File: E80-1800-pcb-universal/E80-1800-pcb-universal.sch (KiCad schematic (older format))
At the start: 48 parts, among them J1 SPI, J2 OLED, J3 USB_C_Receptacle_USB2.0, J4 BATT, Q1 AO3400A, SW1 RST, SW2 BOOT, U1 SRV05-4, U2 XC6206P332MR, U3 STM32F072RBTx

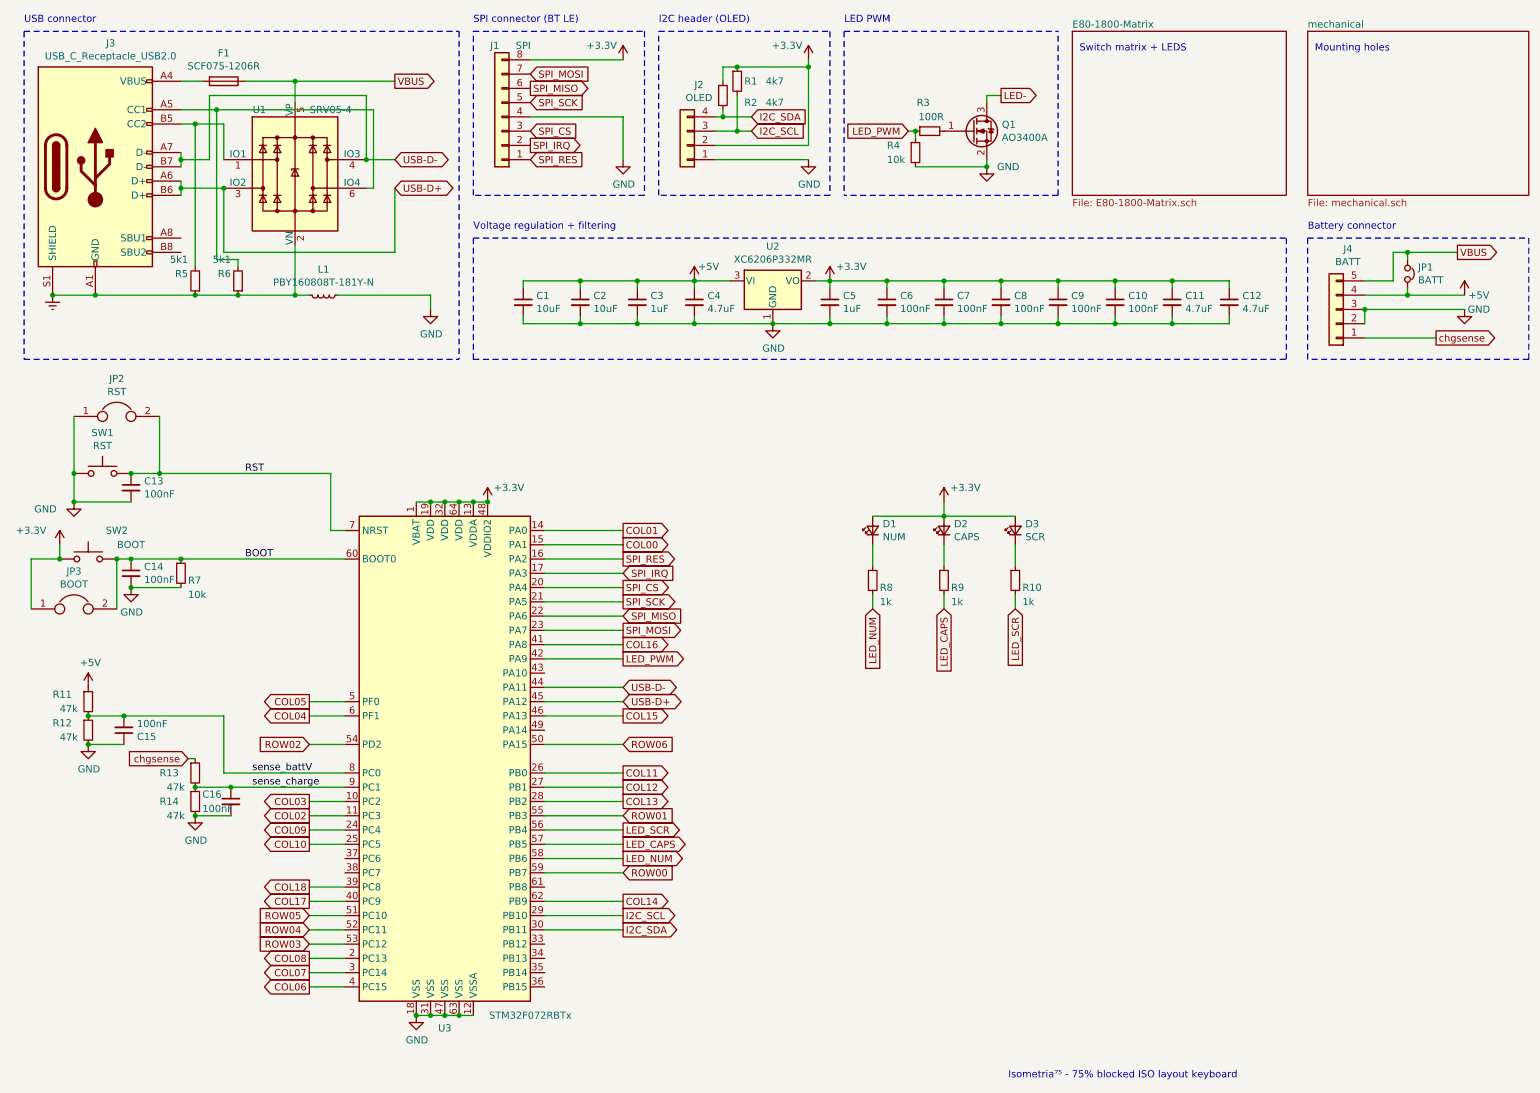
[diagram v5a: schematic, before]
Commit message: increased readability, added missing cap
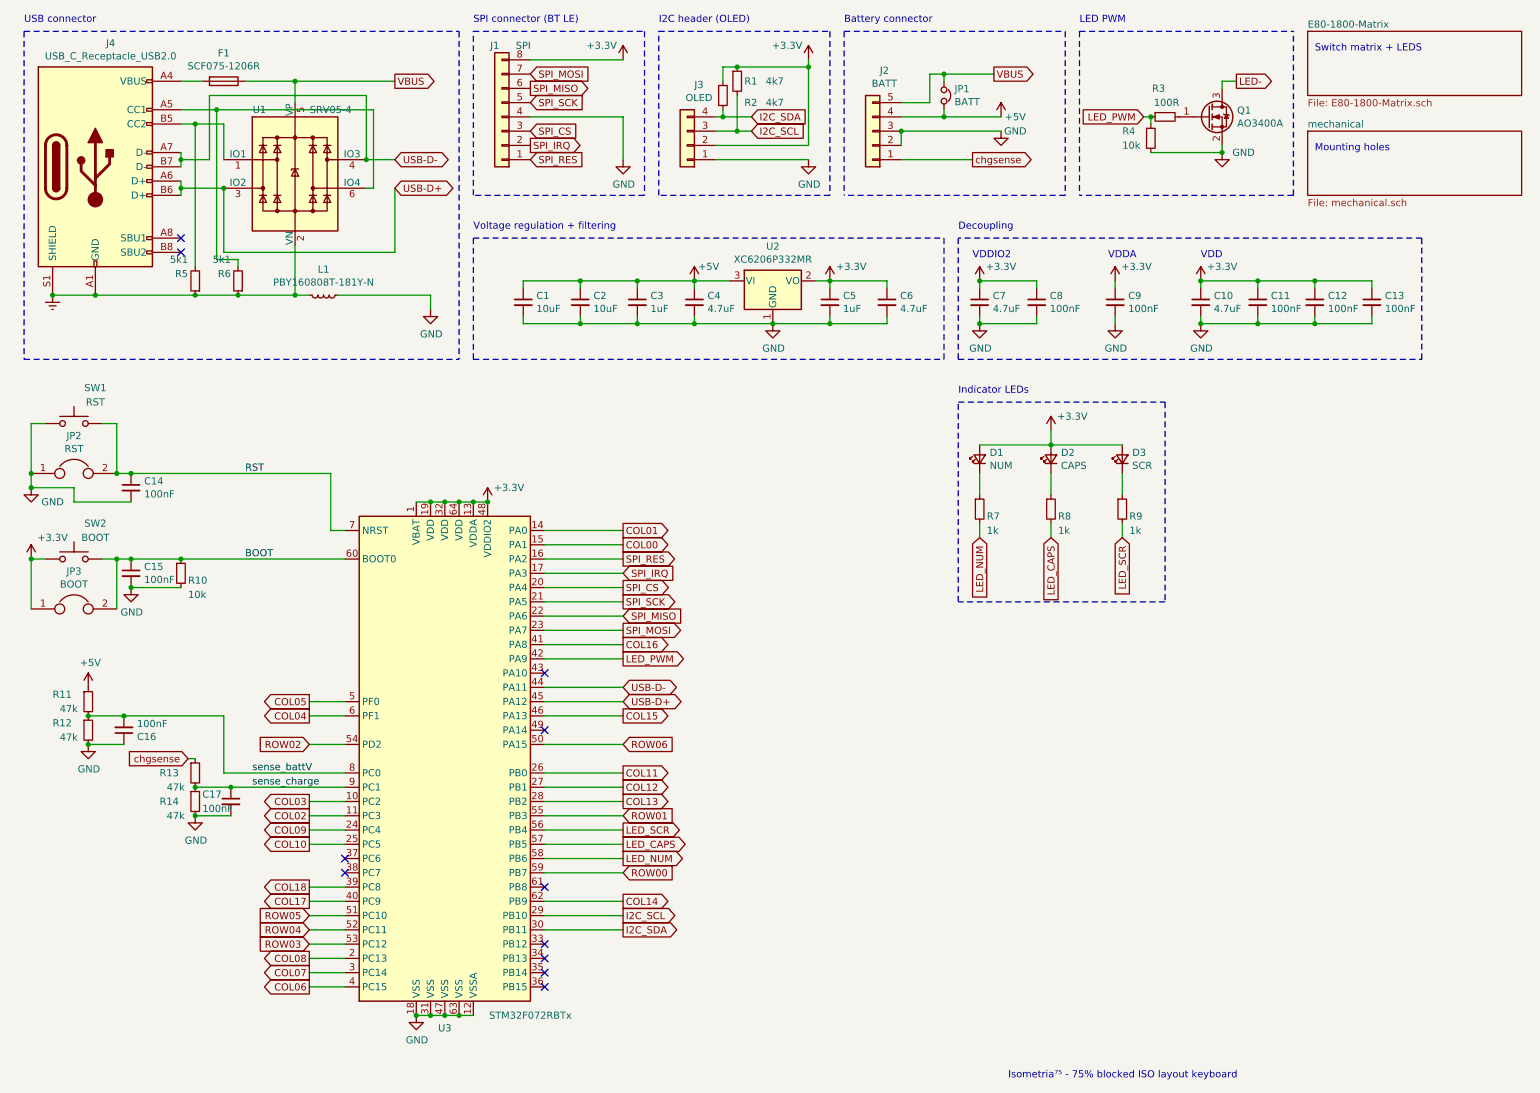
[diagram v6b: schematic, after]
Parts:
- added C7: 4.7uF, kicad-keyboard-parts:C_0603_1608Metric_stealth, symbol Device:C_Small
- renumbered C11 to C10, C10 to C11, C9 to C12, C8 to C13, C13 to C14, C14 to C15, C15 to C16, C16 to C17, C12 to C6, C6 to C8, C7 to C9, J4 to J2, J2 to J3, J3 to J4, R7 to R10, R8 to R7, R9 to R8, R10 to R9
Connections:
- net +3V3: now also C7.1
- net GND: now also C7.2
- no-connect marks 0 -> 11
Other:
- note added: "Decoupling"
- note added: "Indicator LEDs"
- note added: "VDD"
- note added: "VDDA"
- note added: "VDDIO2"
- moved on the sheet: C10, C11, C12, C13, C6, C8, C9, D1, D2, D3, J2, JP1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

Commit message: moved 4u7 to a better spot
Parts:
- removed C6: 4.7uF, kicad-keyboard-parts:C_0603_1608Metric_stealth, symbol Device:C_Small
- renumbered C11 to C10, C12 to C11, C13 to C12, C14 to C13, C15 to C14, C16 to C15, C17 to C16, C7 to C6, C8 to C7, C9 to C8, C10 to C9
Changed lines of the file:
@@
 $EndComp
 $Comp
-L Device:C_Small C17
+L Device:C_Small C16
 U 1 1 5E7D4A32
 P 2000 6050
-F 0 "C17" H 1800 6100 50  0000 L CNN
+F 0 "C16" H 1800 6100 50  0000 L CNN
 F 1 "100nF" H 1800 6000 50  0000 L CNN
 F 2 "kicad-keyboard-parts:C_0603_1608Metric_stealth" H 2000 6050 50  0001 C CNN
@@
 	1    0    0    -1
 $EndComp
-Wire Wire Line
-	6600 2700 6600 2650
 Connection ~ 5800 2700
 Connection ~ 6200 2400
@@
 $EndComp
 $Comp
-L Device:C_Small C10
+L Device:C_Small C9
 U 1 1 5E62B05E
 P 8800 2550
-F 0 "C10" H 8892 2596 50  0000 L CNN
+F 0 "C9" H 8892 2596 50  0000 L CNN
 F 1 "4.7uF" H 8892 2505 50  0000 L CNN
 F 2 "kicad-keyboard-parts:C_0603_1608Metric_stealth" H 8800 2550 50  0001 C CNN
@@
 $EndComp
 $Comp
-L Device:C_Small C12
+L Device:C_Small C11
 U 1 1 5E62A663
 P 9600 2550
-F 0 "C12" H 9692 2596 50  0000 L CNN
+F 0 "C11" H 9692 2596 50  0000 L CNN
 F 1 "100nF" H 9692 2505 50  0000 L CNN
 F 2 "kicad-keyboard-parts:C_0603_1608Metric_stealth" H 9600 2550 50  0001 C CNN
@@
 $EndComp
 $Comp
-L Device:C_Small C13
+L Device:C_Small C12
 U 1 1 5E62A020
 P 10000 2550
-F 0 "C13" H 10092 2596 50  0000 L CNN
+F 0 "C12" H 10092 2596 50  0000 L CNN
 F 1 "100nF" H 10092 2505 50  0000 L CNN
 F 2 "kicad-keyboard-parts:C_0603_1608Metric_stealth" H 10000 2550 50  0001 C CNN
@@
 $EndComp
 $Comp
-L Device:C_Small C9
+L Device:C_Small C8
 U 1 1 5E629144
 P 8200 2550
-F 0 "C9" H 8292 2596 50  0000 L CNN
+F 0 "C8" H 8292 2596 50  0000 L CNN
 F 1 "100nF" H 8292 2505 50  0000 L CNN
 F 2 "kicad-keyboard-parts:C_0603_1608Metric_stealth" H 8200 2550 50  0001 C CNN
@@
 $EndComp
 $Comp
-L Device:C_Small C8
+L Device:C_Small C7
 U 1 1 5E627ED9
 P 7650 2550
-F 0 "C8" H 7742 2596 50  0000 L CNN
+F 0 "C7" H 7742 2596 50  0000 L CNN
 F 1 "100nF" H 7742 2505 50  0000 L CNN
 F 2 "kicad-keyboard-parts:C_0603_1608Metric_stealth" H 7650 2550 50  0001 C CNN
@@
 Wire Wire Line
 	6200 2650 6200 2700
-Connection ~ 6200 2700
-Wire Wire Line
-	6600 2450 6600 2400
 Wire Notes Line style solid
 	3700 2950 3700 2100
@@
 	5250 2650 5250 2700
 Connection ~ 5250 2700
-$Comp
-L Device:C_Small C6
-U 1 1 5E758D9A
-P 6600 2550
-F 0 "C6" H 6692 2596 50  0000 L CNN
-F 1 "4.7uF" H 6692 2505 50  0000 L CNN
-F 2 "kicad-keyboard-parts:C_0603_1608Metric_stealth" H 6600 2550 50  0001 C CNN
-F 3 "~" H 6600 2550 50  0001 C CNN
-F 4 "C19666" H 6600 2550 50  0001 C CNN "LCSC"
-	1    6600 2550
-	1    0    0    -1
-$EndComp
-Wire Wire Line
-	6200 2400 6600 2400
-Wire Wire Line
-	6200 2700 6600 2700
 Wire Wire Line
 	5800 2700 6200 2700
@@
 $EndComp
 $Comp
-L Device:C_Small C15
+L Device:C_Small C14
 U 1 1 5E73CE8B
 P 1300 4450
-F 0 "C15" H 1392 4496 50  0000 L CNN
+F 0 "C14" H 1392 4496 50  0000 L CNN
 F 1 "100nF" H 1392 4405 50  0000 L CNN
 F 2 "kicad-keyboard-parts:C_0603_1608Metric_stealth" H 1300 4450 50  0001 C CNN
@@
 $EndComp
 $Comp
-L Device:C_Small C16
+L Device:C_Small C15
 U 1 1 5E8EC668
 P 1250 5550
-F 0 "C16" H 1342 5596 50  0000 L CNN
+F 0 "C15" H 1342 5596 50  0000 L CNN
 F 1 "100nF" H 1342 5505 50  0000 L CNN
 F 2 "kicad-keyboard-parts:C_0603_1608Metric_stealth" H 1250 5550 50  0001 C CNN
@@
 	4750 5050 4200 5050
 $Comp
-L Device:C_Small C11
+L Device:C_Small C10
 U 1 1 5F6736E1
 P 9200 2550
-F 0 "C11" H 9292 2596 50  0000 L CNN
+F 0 "C10" H 9292 2596 50  0000 L CNN
 F 1 "100nF" H 9292 2505 50  0000 L CNN
 F 2 "kicad-keyboard-parts:C_0603_1608Metric_stealth" H 9200 2550 50  0001 C CNN
@@
 	2700 3750 2700 4150
 $Comp
-L Device:C_Small C14
+L Device:C_Small C13
 U 1 1 5E638A0E
 P 1300 3850
-F 0 "C14" H 1392 3896 50  0000 L CNN
+F 0 "C13" H 1392 3896 50  0000 L CNN
 F 1 "100nF" H 1392 3805 50  0000 L CNN
 F 2 "kicad-keyboard-parts:C_0603_1608Metric_stealth" H 1300 3850 50  0001 C CNN
@@
 Connection ~ 4450 2700
 $Comp
-L Device:C_Small C7
+L Device:C_Small C6
 U 1 1 5F6AB442
 P 7250 2550
-F 0 "C7" H 7342 2596 50  0000 L CNN
+F 0 "C6" H 7342 2596 50  0000 L CNN
 F 1 "4.7uF" H 7342 2505 50  0000 L CNN
 F 2 "kicad-keyboard-parts:C_0603_1608Metric_stealth" H 7250 2550 50  0001 C CNN

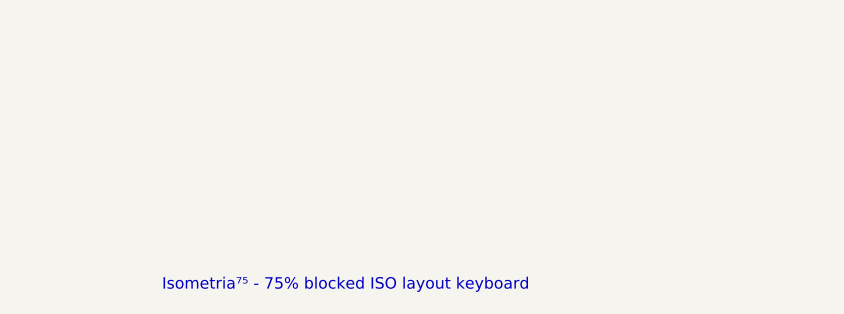
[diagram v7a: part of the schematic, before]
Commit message: removed wrongly placed sch text
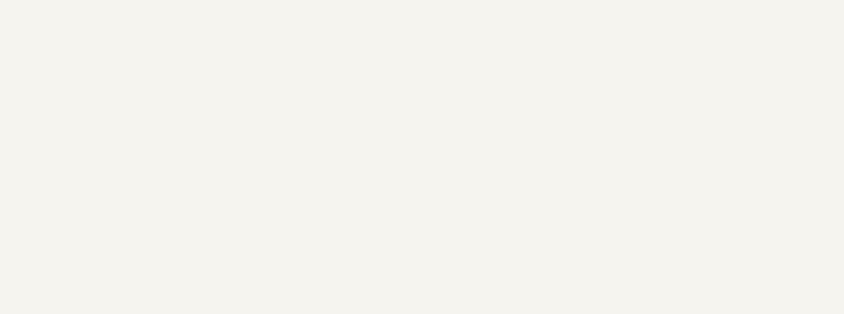
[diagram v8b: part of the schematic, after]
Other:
- note removed: "Isometria⁷⁵ - 75% blocked ISO layout keyboard"
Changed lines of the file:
@@
 	1    0    0    -1
 $EndComp
-Text Notes 7450 8000 0    50   ~ 0
-Isometria⁷⁵ - 75% blocked ISO layout keyboard
 $Comp
 L Connector_Generic:Conn_01x08 J1
@@
 Wire Wire Line
 	4450 2400 4850 2400
-$Sheet
-S 9550 650  1500 450
-U 5ECF9838
-F0 "E80-1800-Matrix" 50
-F1 "E80-1800-Matrix.sch" 50
-$EndSheet
 $Comp
 L MCU_ST_STM32F0:STM32F072RBTx U3
@@
 Connection ~ 1050 2500
 Connection ~ 1750 2500
+$Sheet
+S 9550 650  1500 450
+U 5ECF9838
+F0 "E80-1800-Matrix" 50
+F1 "E80-1800-Matrix.sch" 50
+$EndSheet
 $EndSCHEMATC
